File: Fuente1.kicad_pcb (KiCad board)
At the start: 2 copper layers, 75 x 59.5 mm, 22 parts, among them J1 Alimentacion, J2 Salidas de voltaje, T1 5:1 / 5A, U1 L7812CV, U2 L7912CV, U3 LM338T, U4 L7805CV

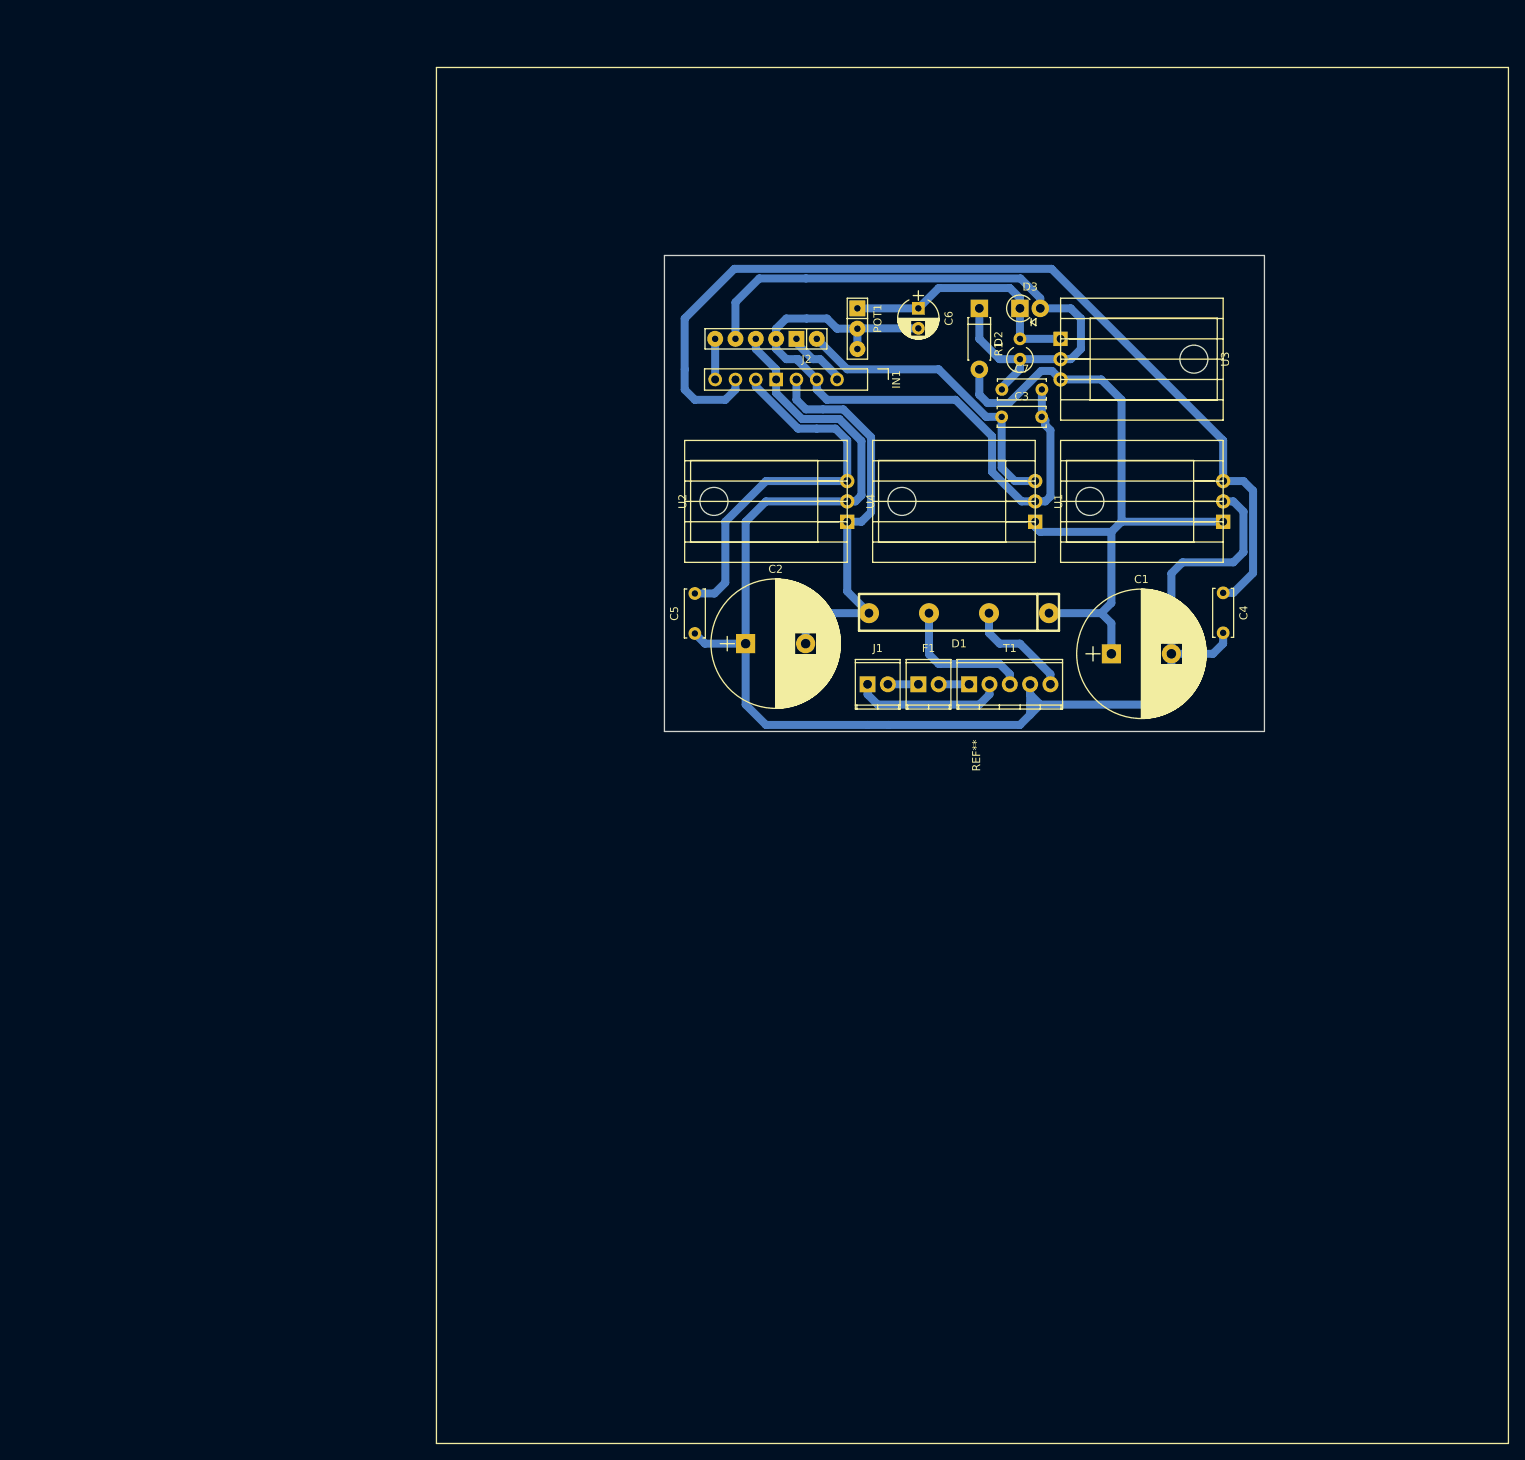
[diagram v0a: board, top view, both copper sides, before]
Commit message: *** Corrección de reguladores ***
 Cambios para hacer commit:
	modificado:    Fuente1.bak
	modificado:    Fuente1.kicad_pcb
	modificado:    Fuente1.kicad_pcb-bak
	modificado:    Fuente1.net
	renombrado:    _saved_Fuente1.sch -> Fuente1.sch
	modificado:    vista1.jpg
	modificado:    vista2.jpg
	nuevo archivo: vista3.jpg
	nuevo archivo: vista4.jpg
	nuevo archivo: vista5.jpg
	nuevo archivo: vista6.jpg
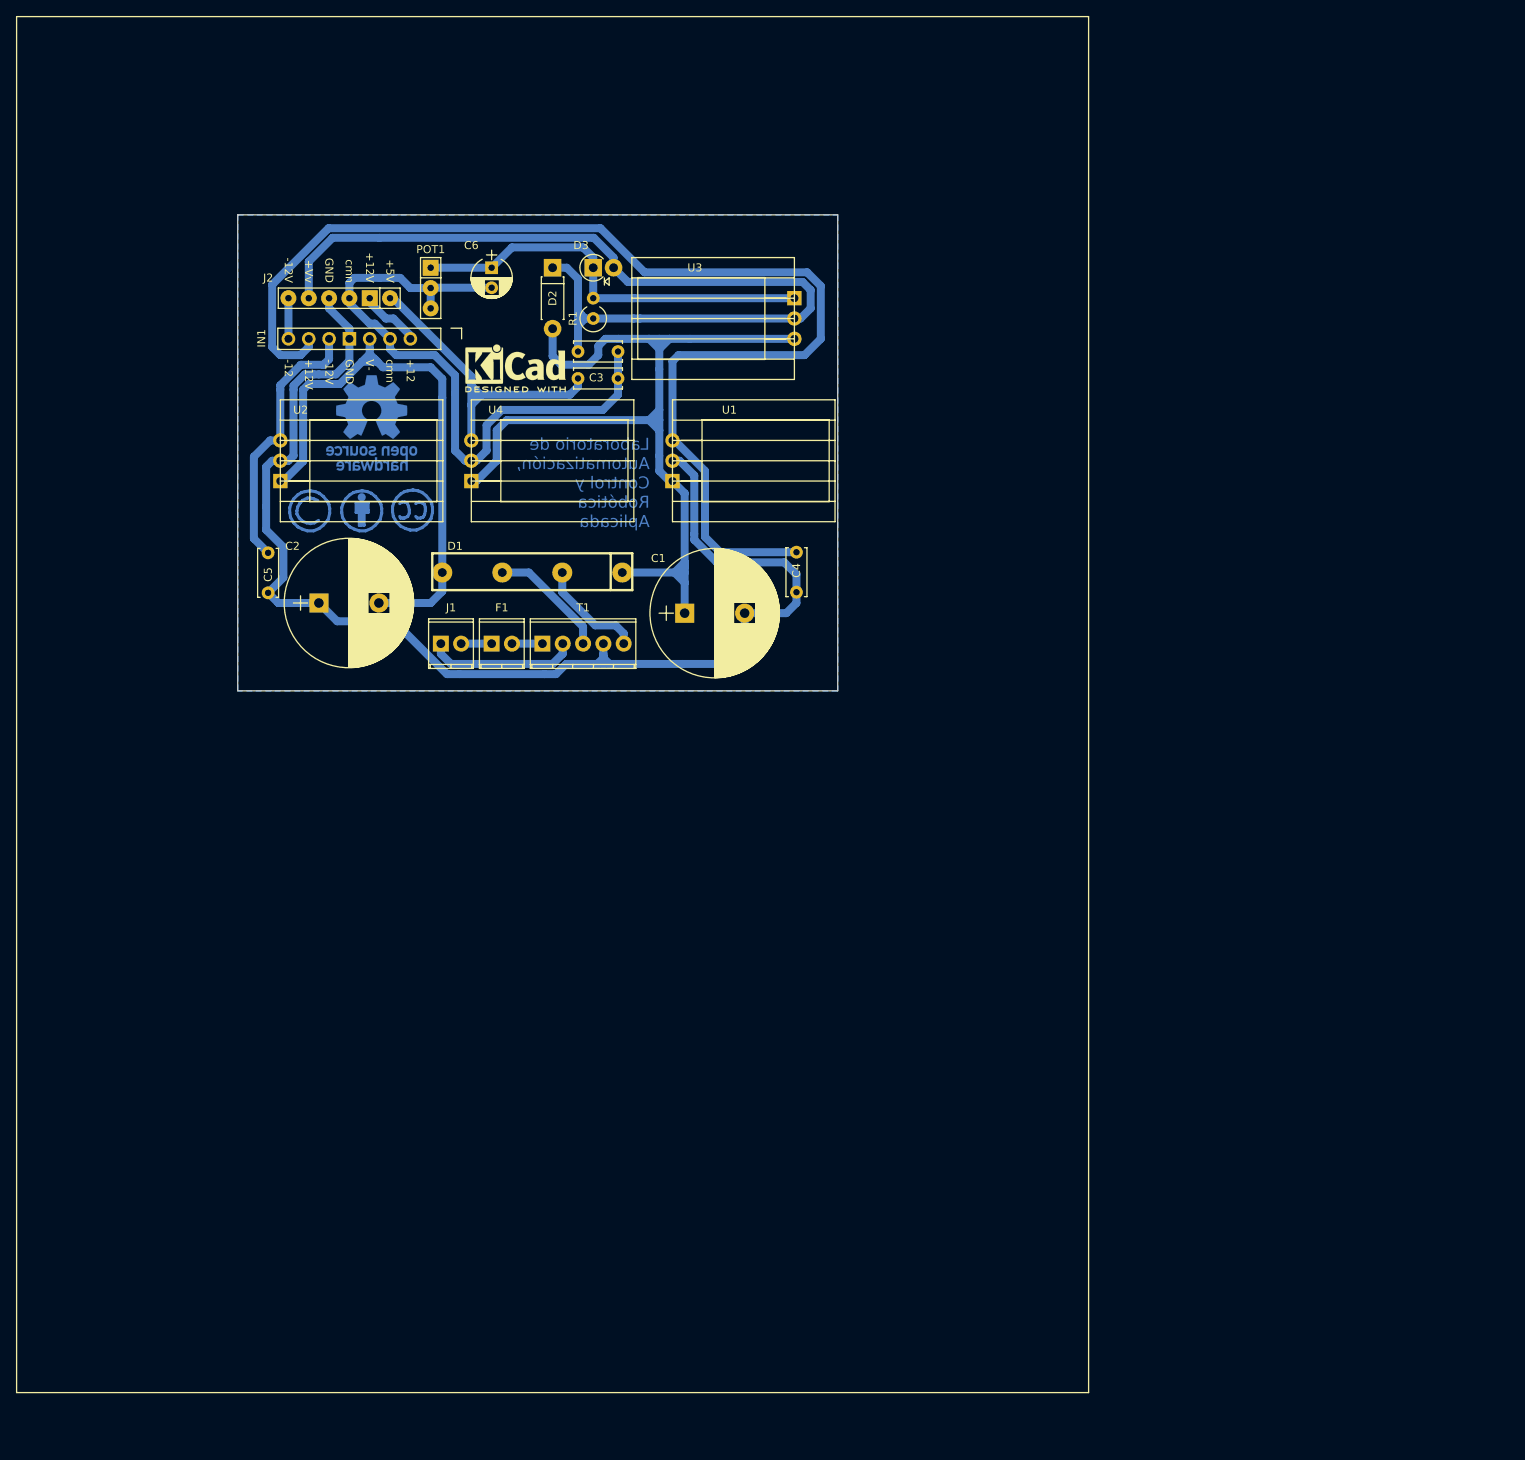
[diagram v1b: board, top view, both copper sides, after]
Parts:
- added REF**: Symbol_CC-ShareAlike_CopperTop_Small, Symbols:Symbol_CC-ShareAlike_CopperTop_Small, B.Cu at (66.2, 79.9)
- added REF**: Symbol_CreativeCommons_CopperTop_Type2_Small, Symbols:Symbol_CreativeCommons_CopperTop_Type2_Small, B.Cu at (79.2, 79.9)
- added REF**: Symbol_CC-Attribution_CopperTop_Small, Symbols:Symbol_CC-Attribution_CopperTop_Small, B.Cu at (72.7, 79.9)
- added REF***: KiCad-Logo2_6mm_SilkScreen, Symbols:KiCad-Logo2_6mm_SilkScreen, F.Cu at (91.9, 62.1)
- added REF***: OSHW-Logo_11.4x12mm_Copper, Symbols:OSHW-Logo_11.4x12mm_Copper, B.Cu at (73.9, 68.9)
- moved U2 71.0 mm to (62.5, 73.7), turned to 270 degrees
- moved U4 70.7 mm to (86.4, 73.7), turned to 270 degrees
- moved U1 69.0 mm to (111.5, 73.7), turned to 270 degrees
- moved D2 53.6 mm to (96.5, 49.5)
- moved C1 53.6 mm to (113.0, 92.7)
- moved C2 53.6 mm to (67.3, 91.4)
- moved C4 53.6 mm to (127.0, 85.1)
- moved C6 53.6 mm to (88.9, 49.5)
- moved D3 53.6 mm to (101.6, 49.5)
- moved F1 53.6 mm to (88.9, 96.5)
- moved IN1 53.6 mm to (83.8, 58.4)
- moved J2 53.6 mm to (69.8, 53.3)
- moved POT1 53.6 mm to (81.3, 52.1)
- moved R1 53.6 mm to (101.6, 55.9)
- moved T1 53.6 mm to (95.2, 96.5)
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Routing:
- net /+Vv: track 78.6 -> 121.0 mm
- net /V+: track 87.5 -> 120.2 mm
- net /+12V: track 121.1 -> 151.0 mm
- net /V-: track 50.6 -> 73.1 mm
- net Net-(C6-Pad1): track 32.1 -> 52.1 mm
- net GND: track 177.9 -> 159.0 mm
- net /-12V: track 49.5 -> 34.7 mm
- net /cmn: track 85.7 -> 82.7 mm
- net Net-(D1-Pad3): track 17.5 -> 15.0 mm
- net /+5V: track 38.4 -> 39.3 mm
- added copper zone on B.Cu, net GND
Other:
- board text added: "+12"
- board text added: "+12V"
- board text added: "+5V"
- board text added: "+Vv"
- board text added: "-12"
- board text added: "-12V"
- board text added: "GND"
- board text added: "Laboratorio de Automatización, Control y Robótica Aplicada"
- board text added: "V-"
- board text added: "cmn"
